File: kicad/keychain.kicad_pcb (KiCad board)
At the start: 2 copper layers, 68 x 64 mm, 53 parts, among them J1 OLED 1.5in SSD1327, J2 LiPo 3.7V, J3 USB-C, SW1 USER1, SW2 USER2, SW3 PWR, SW4 BOOT, SW5 RST, U1 ESP32-C6-MINI-1, U2 MCP73831, U3 AP2112K-3.3, U4 TLV61046A, U5 74AHCT1G125, U6 ESDA6V1-5SC6

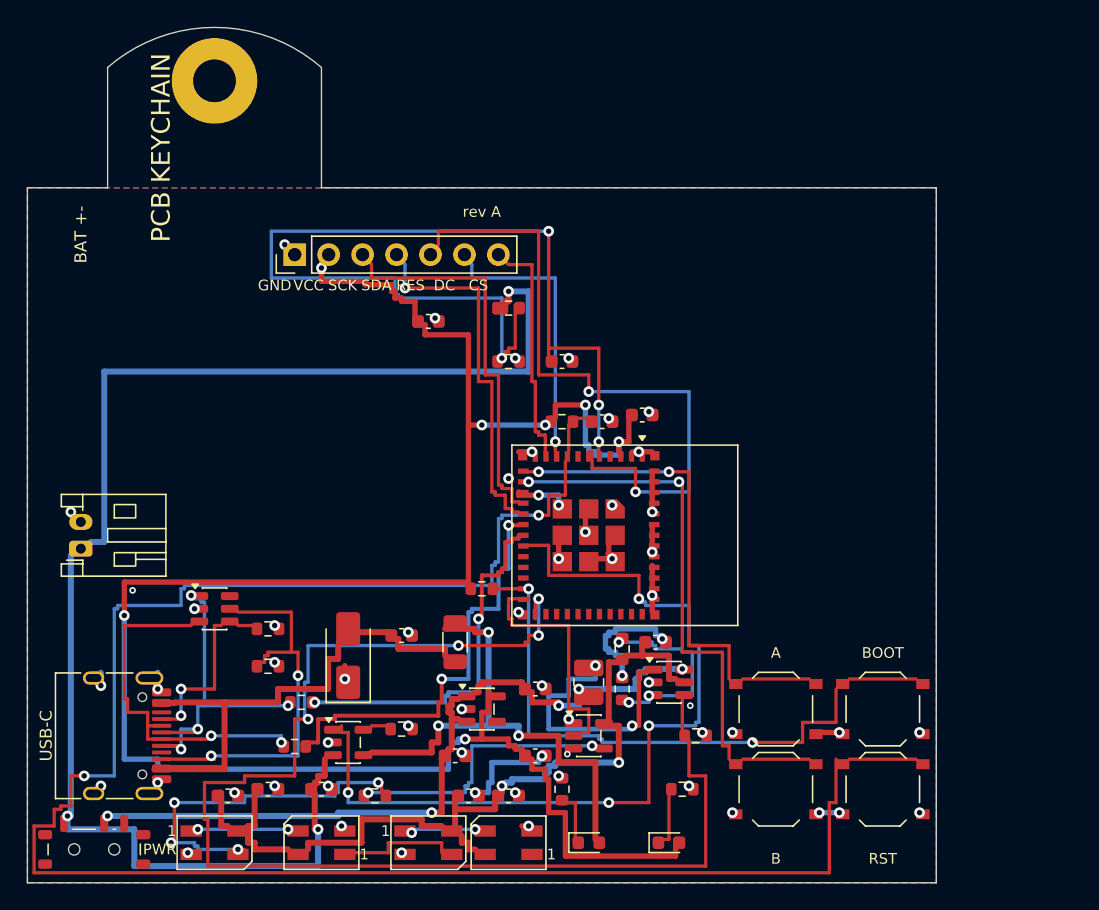
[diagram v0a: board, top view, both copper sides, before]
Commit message: Regenerate PCB placement from e-paper schematic (placement only, no routing)
Replace the obsolete OLED board with a fresh placement generated from the
current ESP32-C6 + 2.36in e-Paper schematic. All 59 schematic footprints
plus an M3 keyring hole are placed with nets assigned; no tracks routed.

Board: 68x38mm rounded outline (fits Waveshare 2.36in panel, under the
72x42mm limit), keyring hole inside the top-left corner, USB-C on the
bottom edge.

- Front: LED1/LED2 (SK6812MINI) at exposed bottom edge
- Back: LED3/LED4 + all circuitry; ESP32 antenna at right edge with
  copper keepout; power block (USB-C, JST, charger, switch) grouped at
  left; e-paper drive grouped above the FPC connector
- tools/place_board.py emits the board; tools/finish_board.py does the
  canonical back-side flip + ref placement via pcbnew; check_placement.py
  verifies same-side courtyard clearance (0 overlaps)

DRC: 0 courtyard overlaps; remaining warnings are silkscreen-adjacent and
the expected unrouted nets (placement only).

Generated with [Devin](https://devin.ai)

Co-Authored-By: Devin <158243242+devin-ai-integration[bot]@users.noreply.github.com>
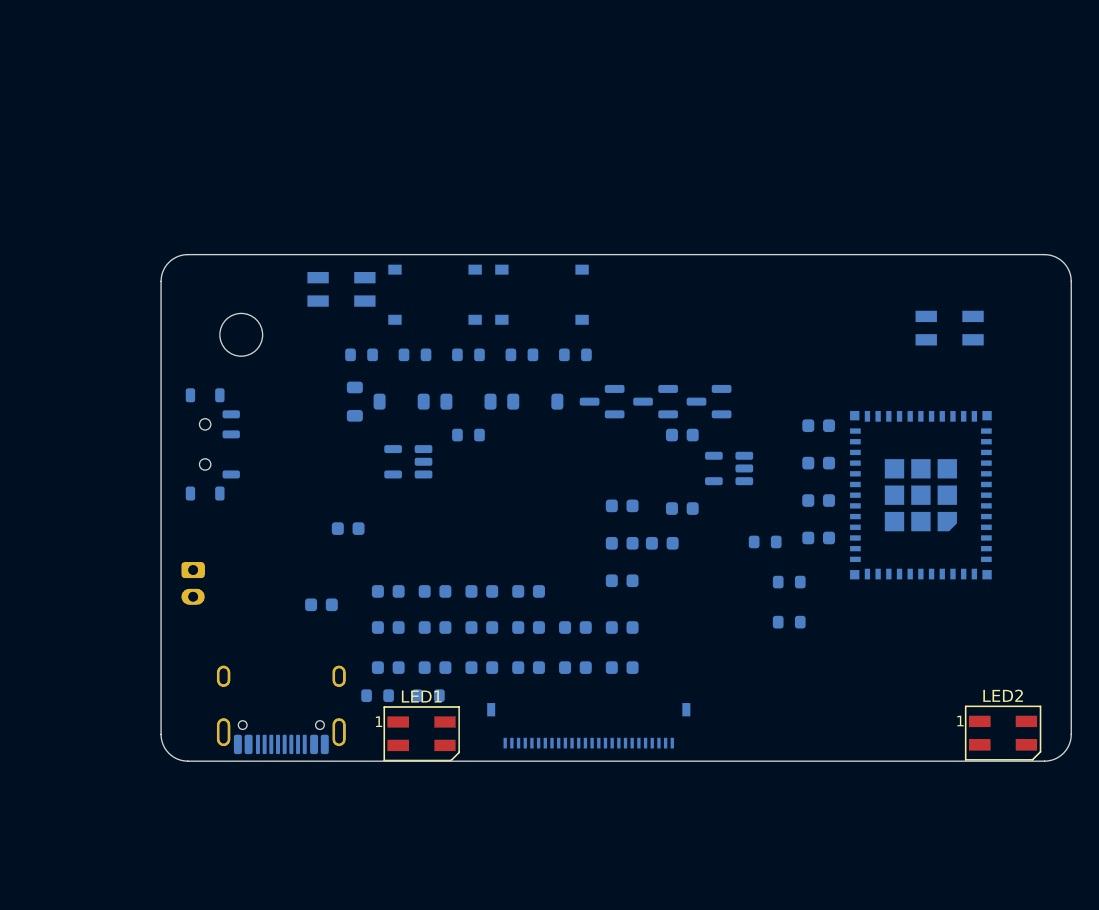
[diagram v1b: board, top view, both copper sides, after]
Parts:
- removed C13: 100nF, Capacitor_SMD:C_0603_1608Metric
- removed F1: 0.5A, Resistor_SMD:R_1206_3216Metric
- removed LED5, LED6: SK6812MINI, LED_SMD:LED_SK6812MINI_PLCC4_3.5x3.5mm_P1.75mm
- removed R12: 97.6k, Resistor_SMD:R_0603_1608Metric
- removed R13: 100k, Resistor_SMD:R_0603_1608Metric
- removed R14: 330, Resistor_SMD:R_0603_1608Metric
- removed R15: 1k, Resistor_SMD:R_0603_1608Metric
- removed SW4: BOOT, Button_Switch_SMD:SW_Push_1P1T_XKB_TS-1187A
- removed SW5: RST, Button_Switch_SMD:SW_Push_1P1T_XKB_TS-1187A
- removed U4: TLV61046A, Package_TO_SOT_SMD:SOT-23-6
- removed U5: 74AHCT1G125, Package_TO_SOT_SMD:SOT-23-5
- removed U6: ESDA6V1-5SC6, Package_TO_SOT_SMD:SOT-23-6
- added C15: 4.7uF, Capacitor_SMD:C_0603_1608Metric, B.Cu at (50.5, 60.9)
- added C16: 1uF, Capacitor_SMD:C_0603_1608Metric, B.Cu at (54.0, 60.9)
- added C17: 1uF, Capacitor_SMD:C_0603_1608Metric, B.Cu at (57.5, 60.9)
- added C18: 1uF, Capacitor_SMD:C_0603_1608Metric, B.Cu at (61.0, 60.9)
- added C19: 1uF, Capacitor_SMD:C_0603_1608Metric, B.Cu at (64.5, 60.9)
- added C20: 1uF, Capacitor_SMD:C_0603_1608Metric, B.Cu at (47.0, 57.9)
- added C21: 1uF, Capacitor_SMD:C_0603_1608Metric, B.Cu at (50.5, 57.9)
- added C22: 1uF, Capacitor_SMD:C_0603_1608Metric, B.Cu at (54.0, 57.9)
- added C23: 1.8uF, Capacitor_SMD:C_0603_1608Metric, B.Cu at (57.5, 57.9)
- added C24: 1uF, Capacitor_SMD:C_0603_1608Metric, B.Cu at (61.0, 57.9)
- added C25: 1uF, Capacitor_SMD:C_0603_1608Metric, B.Cu at (64.5, 57.9)
- added C26: 1uF, Capacitor_SMD:C_0603_1608Metric, B.Cu at (47.0, 55.2)
- added C27: 10uF, Capacitor_SMD:C_0603_1608Metric, B.Cu at (50.5, 55.2)
- added C28: 4.7uF, Capacitor_SMD:C_0603_1608Metric, B.Cu at (54.0, 55.2)
- added C29: 100nF, Capacitor_SMD:C_0603_1608Metric, B.Cu at (79.2, 48.4)
- added D2: MBR0530, Diode_SMD:D_SOD-123, B.Cu at (53.0, 41.0)
- added D3: MBR0530, Diode_SMD:D_SOD-123, B.Cu at (58.0, 41.0)
- added Q1: BSS138, Package_TO_SOT_SMD:SOT-23, B.Cu at (63.0, 41.0)
- added Q2: AO3401A, Package_TO_SOT_SMD:SOT-23, B.Cu at (67.0, 41.0)
- added Q3: S8050, Package_TO_SOT_SMD:SOT-23, B.Cu at (71.0, 41.0)
- C1, C10, C11, C2, C3, C4, C5, C6, C7, LED3, LED4, R1, R2, R8, U1, U2, U3: moved to B.Cu
- C12: value 100nF -> 4.7uF; moved to B.Cu
- C14: value 100nF -> 1uF; moved to B.Cu
- C8, C9: value 10uF -> 100nF; moved to B.Cu
- D1: value SMAJ5.0A -> MBR0530; footprint Diode_SMD:D_SMA -> Diode_SMD:D_SOD-123; moved to B.Cu
- H1: footprint MountingHole:MountingHole_3.2mm_M3_Pad -> MountingHole:MountingHole_3.2mm_M3; moved to B.Cu
- J1: value OLED 1.5in SSD1327 -> USB-C; footprint Connector_PinHeader_2.54mm:PinHeader_1x07_P2.54mm_Vertical -> Connector_USB:USB_C_Receptacle_HRO_TYPE-C-31-M-12; moved to B.Cu
- J2: value LiPo 3.7V -> LiPo; moved to B.Cu
- J3: value USB-C -> FPC-SMD_FH34SRJ-26S-0.5SH-50; footprint Connector_USB:USB_C_Receptacle_HRO_TYPE-C-31-M-12 -> Hirose_FH34SRJ-26S-0.5SH_1x26-1MP_P0.50mm_Horizontal; moved to B.Cu
- L1: value 2.2uH -> 10uH; footprint Inductor_SMD:L_1008_2520Metric -> Inductor_SMD:L_0805_2012Metric; moved to B.Cu
- LED1: value RED -> SK6812MINI; footprint LED_SMD:LED_0603_1608Metric -> LED_SMD:LED_SK6812MINI_PLCC4_3.5x3.5mm_P1.75mm
- LED2: value GRN -> SK6812MINI; footprint LED_SMD:LED_0603_1608Metric -> LED_SMD:LED_SK6812MINI_PLCC4_3.5x3.5mm_P1.75mm
- R10, R9: value 100k -> 47k; moved to B.Cu
- R11: value 510k -> 10k; moved to B.Cu
- R3: value 22 -> 4.7k; moved to B.Cu
- R4: value 22 -> 10k; moved to B.Cu
- R5: value 4.7k -> 1M; moved to B.Cu
- R6: value 1k -> 0.2; moved to B.Cu
- R7: value 10k -> 5M; moved to B.Cu
- SW1: value USER1 -> PWR; footprint Button_Switch_SMD:SW_Push_1P1T_XKB_TS-1187A -> Button_Switch_SMD:SW_SPDT_Shouhan_MSK12C02; moved to B.Cu
- SW2: value USER2 -> BOOT; moved to B.Cu
- SW3: value PWR -> USER; footprint Button_Switch_SMD:SW_SPDT_Shouhan_MSK12C02 -> Button_Switch_SMD:SW_Push_1P1T_XKB_TS-1187A; moved to B.Cu
- moved LED4 60.8 mm to (89.0, 35.5)
- moved SW3 53.3 mm to (58.5, 33.0), turned to 180 degrees
- moved SW1 47.1 mm to (33.3, 44.2), turned to 90 degrees
- moved SW2 44.9 mm to (50.5, 33.0), turned to 180 degrees
- moved LED3 42.5 mm to (43.5, 32.6), turned to 180 degrees
- moved R4 39.0 mm to (77.0, 54.5), turned to 180 degrees
- moved C10 37.6 mm to (67.5, 51.6), turned to 180 degrees
- moved J3 36.0 mm to (62.0, 65.3), turned to 0 degrees
- moved R6 34.3 mm to (49.0, 37.5), turned to 180 degrees
- moved J1 32.6 mm to (39.0, 62.6), turned to 0 degrees
- moved C11 30.8 mm to (64.5, 54.4), turned to 180 degrees
- moved C3 29.4 mm to (69.0, 43.5), turned to 180 degrees
- moved R5 28.2 mm to (45.0, 37.5), turned to 180 degrees
- moved L1 27.3 mm to (44.5, 41.0), turned to -90 degrees
- moved LED2 26.3 mm to (93.0, 65.8)
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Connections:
- net LED_C1 renamed /LED_C3
- C1 pad 1: VBUS -> GND
- C1 pad 2: GND -> VBUS
- C10 pad 1: +5V -> GND
- C10 pad 2: GND -> /VBAT_SW
- C11 pad 1: +5V -> GND
- C11 pad 2: GND -> /VBAT_SW
- C12 pad 1: +5V -> /EPD_CP
- C12 pad 2: GND -> /EPD_LX
- C14 pad 1: +3V3 -> GND
- C14 pad 2: GND -> /EPD_VGH
- C2 pad 1: VBAT -> GND
- C2 pad 2: GND -> +BATT
- C3 pad 1: VBAT_SYS -> GND
- C3 pad 2: GND -> /VBAT_SW
- C4 pad 1: +3V3 -> GND
- C4 pad 2: GND -> +3V3
- C5 pad 1: +3V3 -> GND
- C5 pad 2: GND -> +3V3
- C6 pad 1: EN -> GND
- C6 pad 2: GND -> +3V3
- C7 pad 1: BAT_ADC -> GND
- C7 pad 2: GND -> /EN
- C8 pad 1: VBAT_SYS -> GND
- C8 pad 2: GND -> /VBAT_SW
- C9 pad 1: +5V -> GND
- C9 pad 2: GND -> /VBAT_SW
- D1 pad 1: GND -> /EPD_VGH
- D1 pad 2: VBUS -> /EPD_LX
- J2 pad 1: VBAT -> +BATT
- L1 pad 1: VBAT_SYS -> /EPD_LX
- L1 pad 2: BOOST_SW -> /VCC
- LED1 pad 1: CHG_LED -> /LED_C1
- LED1 pad 2: VBUS_F -> GND
- LED2 pad 1: PWR_LED -> /LED_C2
- LED2 pad 2: +3V3 -> GND
- LED3 pad 3: LED_D0 -> /LED_C2
- LED3 pad 4: +5V -> /VBAT_SW
- LED4 pad 1: LED_C2 -> unconnected-(LED4-DOUT-Pad1)
- LED4 pad 4: +5V -> /VBAT_SW
- R1 pad 1: CC1 -> GND
- R1 pad 2: GND -> /CC1
- R10 pad 1: BAT_ADC -> GND
- R10 pad 2: GND -> /EPD_GB
- R11 pad 1: +5V -> /IO8
- R11 pad 2: LED_FB -> +3V3
- R2 pad 1: CC2 -> GND
- R2 pad 2: GND -> /CC2
- R3 pad 1: USB_DP_CONN -> GND
- R3 pad 2: USB_DP -> /PROG
- R4 pad 1: USB_DM_CONN -> /EN
- R4 pad 2: USB_DM -> +3V3
- R5 pad 1: PROG -> GND
- R5 pad 2: GND -> /EPD_GDR
- R6 pad 1: CHG_LED -> GND
- R6 pad 2: GND -> /EPD_SNS
- R7 pad 1: +3V3 -> GND
- R7 pad 2: EN -> /EPD_VCOM
- R8 pad 1: +3V3 -> /EPD_GB
- R8 pad 2: BOOT -> /EPD_EN
- R9 pad 1: VBAT -> /EPD_GATE
- R9 pad 2: BAT_ADC -> +3V3
- SW1 pad 1: USER1 -> +BATT
- SW1 pad 2: GND -> /VBAT_SW
- SW2 pad 1: USER2 -> /BTN_BOOT
- SW3 pad 1: VBAT -> /BTN_USER
- SW3 pad 2: VBAT_SYS -> GND
- U1 pad 10: OLED_CS -> unconnected-(U1-IO5-Pad10)
- U1 pad 12: USER1 -> /BTN_USER
- U1 pad 13: USER2 -> unconnected-(U1-IO1-Pad13)
- U1 pad 15: OLED_SCK -> /EPD_EN
- U1 pad 16: OLED_MOSI -> unconnected-(U1-IO7-Pad16)
- U1 pad 17: USB_DM -> /USB_DM
- U1 pad 18: USB_DP -> /USB_DP
- U1 pad 19: CHG_STAT -> unconnected-(U1-IO14-Pad19)
- U1 pad 20: (no net) -> unconnected-(U1-IO15-Pad20)
- U1 pad 21: (no net) -> unconnected-(U1-NC-Pad21)
- U1 pad 22: (no net) -> /IO8
- U1 pad 23: BOOT -> /BTN_BOOT
- U1 pad 24: LED_DAT_3V -> /EPD_SCK
- U1 pad 25: BOOST_EN -> /EPD_DIN
- U1 pad 26: (no net) -> /EPD_CS
- U1 pad 27: (no net) -> /EPD_DC
- U1 pad 28: (no net) -> /EPD_RST
- U1 pad 29: (no net) -> /EPD_BUSY
- U1 pad 30: (no net) -> unconnected-(U1-RXD0-Pad30)
- U1 pad 31: (no net) -> unconnected-(U1-TXD0-Pad31)
- U1 pad 32: (no net) -> unconnected-(U1-NC-Pad32)
- U1 pad 33: (no net) -> unconnected-(U1-NC-Pad33)
- U1 pad 34: (no net) -> unconnected-(U1-NC-Pad34)
- U1 pad 35: (no net) -> unconnected-(U1-NC-Pad35)
- U1 pad 4: (no net) -> unconnected-(U1-NC-Pad4)
- U1 pad 5: BAT_ADC -> /LED_DIN
- U1 pad 6: OLED_RES -> unconnected-(U1-IO3-Pad6)
- U1 pad 7: (no net) -> unconnected-(U1-NC-Pad7)
- U1 pad 8: EN -> /EN
- U1 pad 9: OLED_DC -> unconnected-(U1-IO4-Pad9)
- U2 pad 1: CHG_STAT -> unconnected-(U2-STAT-Pad1)
- U2 pad 3: VBAT -> +BATT
- U2 pad 4: VBUS_F -> VBUS
- U2 pad 5: PROG -> /PROG
- U3 pad 1: VBAT_SYS -> /VBAT_SW
- U3 pad 3: VBAT_SYS -> /VBAT_SW
- U3 pad 4: (no net) -> unconnected-(U3-NC-Pad4)
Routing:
- net +3V3: track 155.5 -> 0.00 mm, vias 7 -> 0
- net EN: track 149.9 -> 0.00 mm, vias 2 -> 0
- net VBAT: track 110.0 -> 0.00 mm, vias 3 -> 0
- net GND: track 99.6 -> 0.00 mm, vias 61 -> 0
- net BOOST_EN: track 99.2 -> 0.00 mm, vias 4 -> 0
- net BAT_ADC: track 75.2 -> 0.00 mm, vias 4 -> 0
- net +5V: track 67.8 -> 0.00 mm, vias 2 -> 0
- net CHG_STAT: track 65.3 -> 0.00 mm, vias 4 -> 0
- net VBAT_SYS: track 60.5 -> 0.00 mm, vias 5 -> 0
- net OLED_RES: track 51.0 -> 0.00 mm, vias 2 -> 0
- net VBUS: track 50.7 -> 0.00 mm
- net BOOT: track 47.3 -> 0.00 mm, vias 2 -> 0
- net USER2: track 42.4 -> 0.00 mm, vias 2 -> 0
- net VBUS_F: track 39.3 -> 0.00 mm, vias 3 -> 0
- net USER1: track 37.1 -> 0.00 mm, vias 2 -> 0
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- removed copper zone on B.Cu, net GND
- removed copper zone on F.Cu, net GND
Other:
- board size 68 x 64 mm -> 68.1 x 37.9 mm
- board text added: "USER"
- board text added: "rev B - e-Paper"
- board text removed: "A"
- board text removed: "B"
- board text removed: "BAT +-"
- board text removed: "CS"
- board text removed: "DC"
- board text removed: "GND"
- board text removed: "PWR"
- board text removed: "RES"
- board text removed: "RST"
- board text removed: "SCK"
- board text removed: "SDA"
- board text removed: "USB-C"
- board text removed: "VCC"
- board text removed: "rev A"
